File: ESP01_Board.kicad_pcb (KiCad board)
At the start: 2 copper layers, 40 x 30 mm, 64 parts, among them J1 Conn_01x02, J10 Vin, J2 Conn_01x02, J3 IN, J4 IN, J5 DHT11/22, J6 Conn_01x02, J7 IN, J8 RELAY, J9 USB_C_Receptacle_PowerOnly_6P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

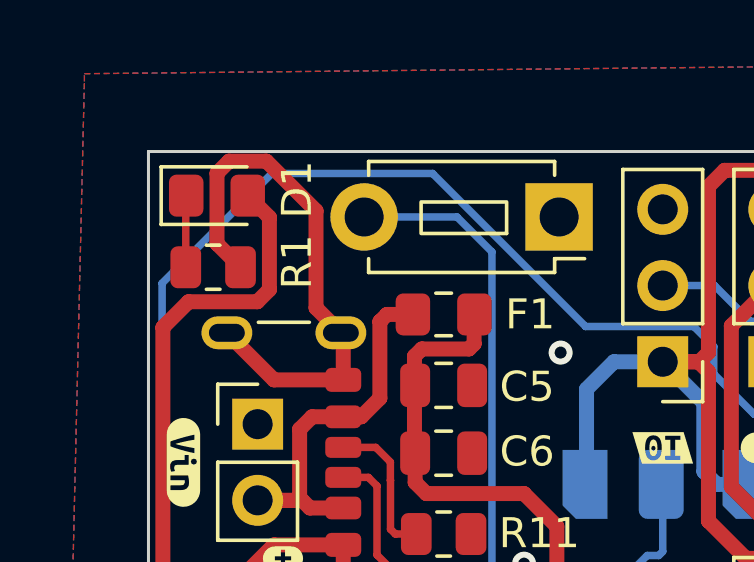
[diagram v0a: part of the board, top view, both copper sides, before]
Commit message: Conclusa la prima versione
 - Inserite le serigrafie e controllato il circuito
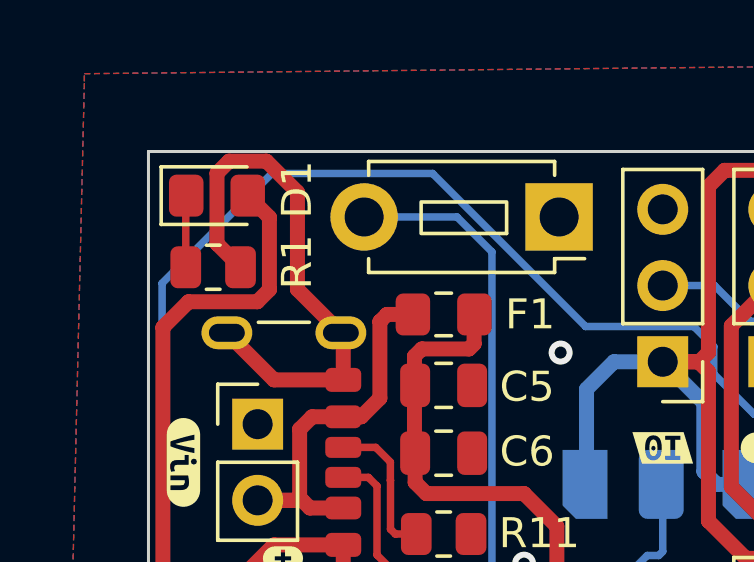
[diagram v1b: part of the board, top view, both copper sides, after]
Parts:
- removed kibuzzard-6669C9CC: G***, kibuzzard-6669C9CC
- added kibuzzard-6669D1CD: G***, kibuzzard-6669D1CD, B.Cu at (140.2, 91.7)

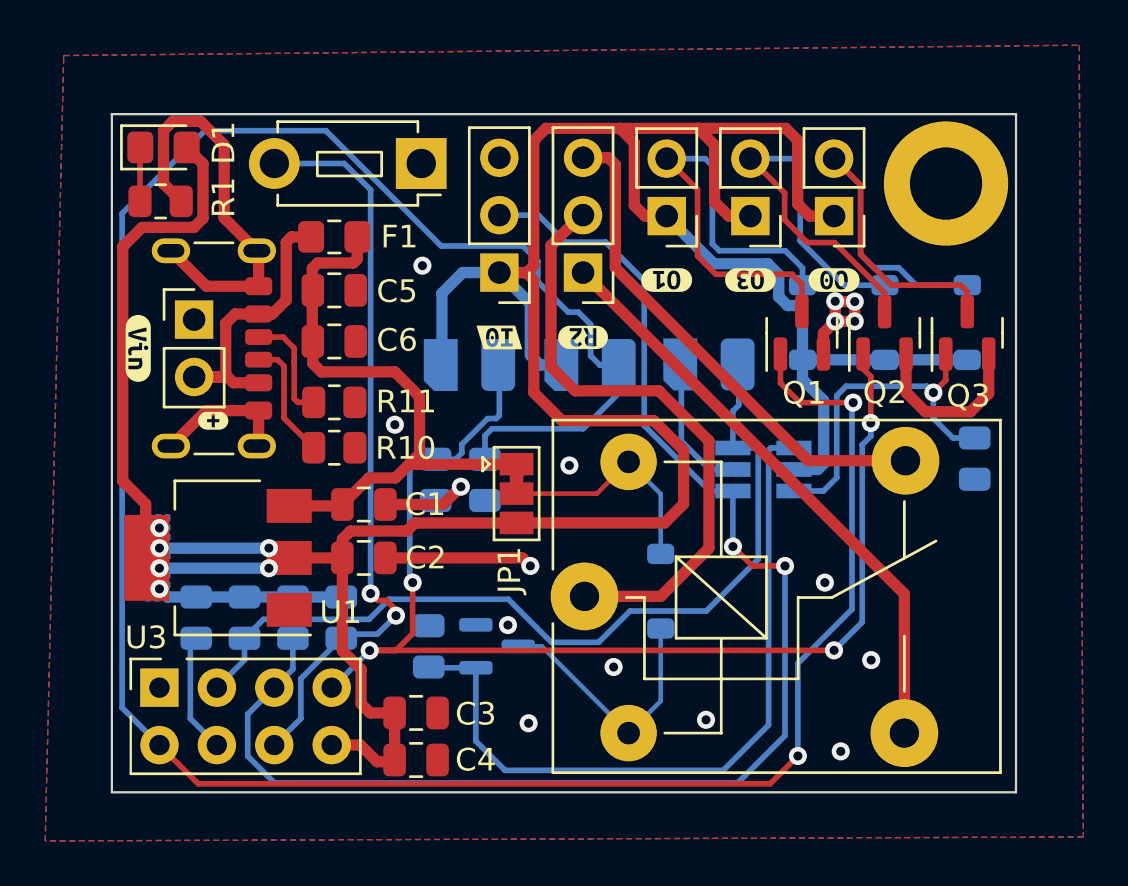
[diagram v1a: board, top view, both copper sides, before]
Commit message: Modificato lo stadio di ingresso
 - Aggiunti i D-latch per l'utilizzo dei due GPIO di strapping

 - Corretto il Cartiglio dello schematico e compilato quello del foglio del PCB
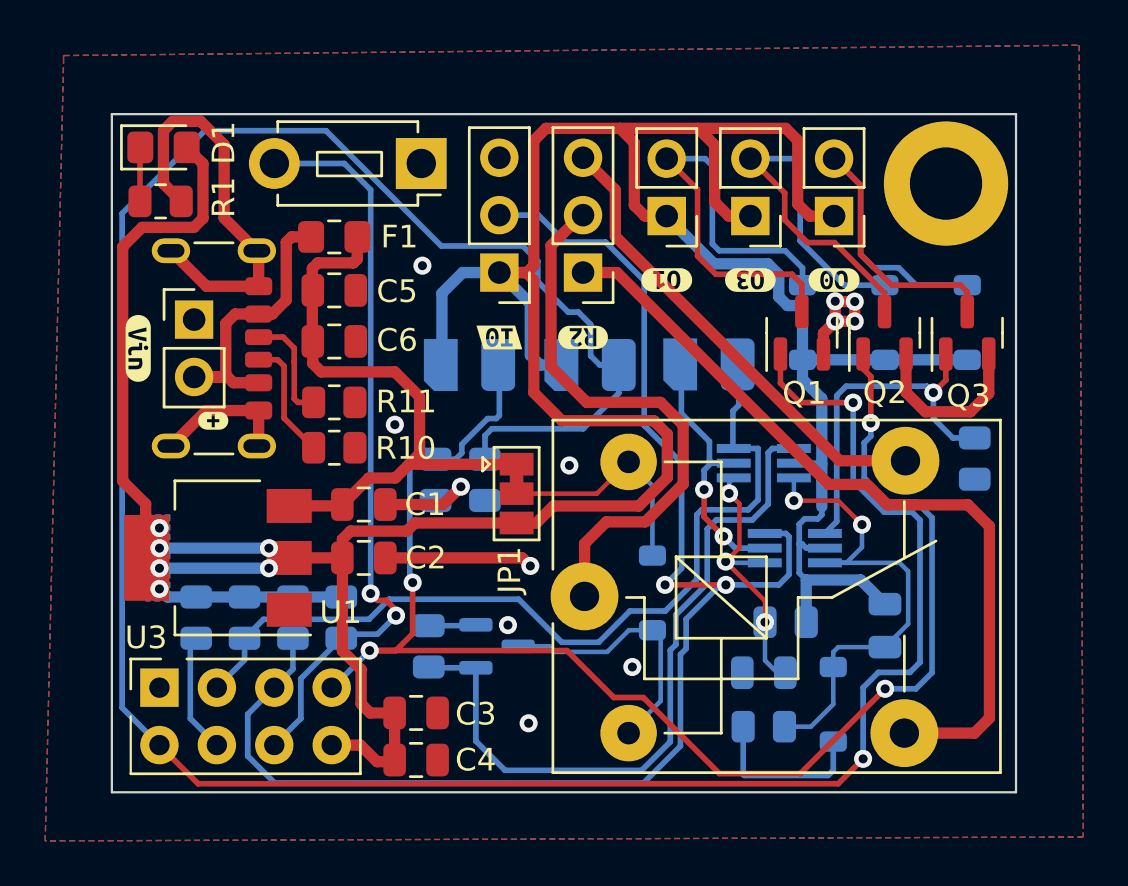
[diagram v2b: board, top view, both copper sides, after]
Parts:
- removed kibuzzard-6669D1CD: G***, kibuzzard-6669D1CD
- added C7: 10u, Capacitor_SMD:C_0805_2012Metric, B.Cu at (158.8, 106.1)
- added C8: 10u, Capacitor_SMD:C_0805_2012Metric, B.Cu at (164.2, 104.0)
- added D6: 1N4148, Diode_SMD:D_SOD-123, B.Cu at (161.9, 107.5)
- added R12: 56k, Resistor_SMD:R_0805_2012Metric, B.Cu at (159.8, 103.9)
- added R13: 56k, Resistor_SMD:R_0805_2012Metric, B.Cu at (158.8, 108.5)
- added U4: ~, Package_TO_SOT_SMD:SOT-363_SC-70-6_Handsoldering, B.Cu at (158.8, 96.9)
- added kibuzzard-666AF5FD: G***, kibuzzard-666AF5FD, B.Cu at (140.2, 91.7)
- U2: value 74LVC2G04 -> ~; footprint Package_TO_SOT_SMD:SOT-23-6_Handsoldering -> Package_TO_SOT_SMD:SOT-363_SC-70-6_Handsoldering
- moved U2 3.75 mm to (160.2, 100.6)
- moved D5 0.37 mm to (153.9, 102.6)
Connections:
- U2 pad 1: /GPIO0 -> /RC-
- U2 pad 3: /GPIO2 -> /GPIO0
- U2 pad 4: Net-(Q4-G) -> Net-(Q3-G)
- U2 pad 6: Net-(Q3-G) -> /RC+
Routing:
- net /RC+: track 0.00 -> 22.3 mm, vias 0 -> 2
- net GND: track 54.6 -> 70.6 mm, vias 16 -> 14
- net /RC-: track 0.00 -> 11.8 mm, vias 0 -> 3
- net +3V3: track 162.6 -> 173.7 mm
- net /GPIO3: track 54.8 -> 65.6 mm
- net /Rno: track 26.3 -> 35.2 mm
- net /GPIO1: track 113.3 -> 119.0 mm
- net /Rcom: track 26.8 -> 24.6 mm
- net /GPIO0: track 62.9 -> 65.0 mm
- net /Rnc: track 22.5 -> 21.0 mm
- net Net-(Q4-G): track 33.0 -> 31.8 mm
- net Net-(Q3-G): track 15.6 -> 16.1 mm

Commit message: Cambiati i footprint ai due Latch
 - Probabilmente ho fatto altre modifiche grafiche alla scheda,
 - Ho fatto delle stampe dei layer quindi anche sulle impostazioni qualcosa può essere cambiato
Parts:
- U2, U4: footprint Package_TO_SOT_SMD:SOT-363_SC-70-6_Handsoldering -> Package_TO_SOT_SMD:SOT-363_SC-70-6
- moved kibuzzard-6669B0A4 0.63 mm to (151.1, 94.9)
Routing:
- net GND: track 70.3 -> 75.9 mm, vias 14 -> 15
- net /RC-: track 11.8 -> 12.7 mm
- net /GPIO1: track 119.0 -> 119.7 mm

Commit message: Completata Rev1.1
 - Sistemati Errori di sovrascritture (Vedi ad esempio i cartigli)
 - Sistemata la BOM
 - Corrette le Serigrafie
 - Controllato il design
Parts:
- removed kibuzzard-6669ACBA: G***, kibuzzard-6669ACBA
- removed kibuzzard-6669ACE8: G***, kibuzzard-6669ACE8
- removed kibuzzard-6669ACFC: G***, kibuzzard-6669ACFC
- removed kibuzzard-6669AD07: G***, kibuzzard-6669AD07
- removed kibuzzard-6669AEE9: G***, kibuzzard-6669AEE9
- removed kibuzzard-6669B0A4: G***, kibuzzard-6669B0A4
- removed kibuzzard-6669B0B1: G***, kibuzzard-6669B0B1
- removed kibuzzard-6669B0BF: G***, kibuzzard-6669B0BF
- removed kibuzzard-6669B0CD: G***, kibuzzard-6669B0CD
- removed kibuzzard-6669C294: G***, kibuzzard-6669C294
- removed kibuzzard-6669C59D: G***, kibuzzard-6669C59D
- removed kibuzzard-6669C71F: G***, kibuzzard-6669C71F
- removed kibuzzard-6669C8D3: G***, kibuzzard-6669C8D3
- removed kibuzzard-666AF5FD: G***, kibuzzard-666AF5FD
- added kibuzzard-666D6245: G***, kibuzzard-666D6245, F.Cu at (131.1, 91.8)
- added kibuzzard-666D6261: G***, kibuzzard-666D6261, F.Cu at (150.8, 91.3)
- added kibuzzard-666D6272: G***, kibuzzard-666D6272, F.Cu at (154.5, 88.7)
- added kibuzzard-666D627E: G***, kibuzzard-666D627E, F.Cu at (158.2, 88.7)
- added kibuzzard-666D6286: G***, kibuzzard-666D6286, F.Cu at (161.9, 88.7)
- added kibuzzard-666D62C0: G***, kibuzzard-666D62C0, F.Cu at (147.1, 91.3)
- added kibuzzard-666D62C8: G***, kibuzzard-666D62C8, F.Cu at (134.4, 95.0)
- added kibuzzard-666D62F4: G***, kibuzzard-666D62F4, B.Cu at (141.7, 91.8)
- added kibuzzard-666D6307: G***, kibuzzard-666D6307, B.Cu at (168.1, 105.5)
- added kibuzzard-666D6618: G***, kibuzzard-666D6618, B.Cu at (140.4, 83.6)
- added kibuzzard-666D664B: G***, kibuzzard-666D664B, B.Cu at (156.4, 94.9)
- added kibuzzard-666D6651: G***, kibuzzard-666D6651, B.Cu at (151.1, 94.9)
- added kibuzzard-666D6656: G***, kibuzzard-666D6656, B.Cu at (145.7, 94.9)
- added kibuzzard-666D66A3: G***, kibuzzard-666D66A3, B.Cu at (139.5, 91.8)

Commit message: Aggiunti i codici LCSC + Aggiornato footprint del fuse
 - Aggiunta anche la serigrafia con il valore del fusibile,
 - Aggiornata la data sul foglio del PCB,
 - Ricreati i teardrop
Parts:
- added kibuzzard-666FE76E: G***, kibuzzard-666FE76E, B.Cu at (131.7, 91.8)
- D1: value LED -> LED RED
- F1: value Fuse -> Fuse 1A; footprint Fuse:Fuse_0805_2012Metric_Pad1.15x1.40mm_HandSolder -> Fuse:Fuse_1206_3216Metric_Pad1.42x1.75mm_HandSolder
- R12, R13: value 56k -> 42k
- U2, U4: value ~ -> 74AUP1G373GW
- moved F1 0.74 mm to (140.5, 86.9)
